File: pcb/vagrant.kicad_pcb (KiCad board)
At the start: 2 copper layers, 169.5 x 90.2 mm, 35 parts, among them K1 KEYSW, K10 KEYSW, K2 KEYSW, K3 KEYSW, K4 KEYSW, K5 KEYSW, K6 KEYSW, K7 KEYSW, K8 KEYSW, K9 KEYSW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

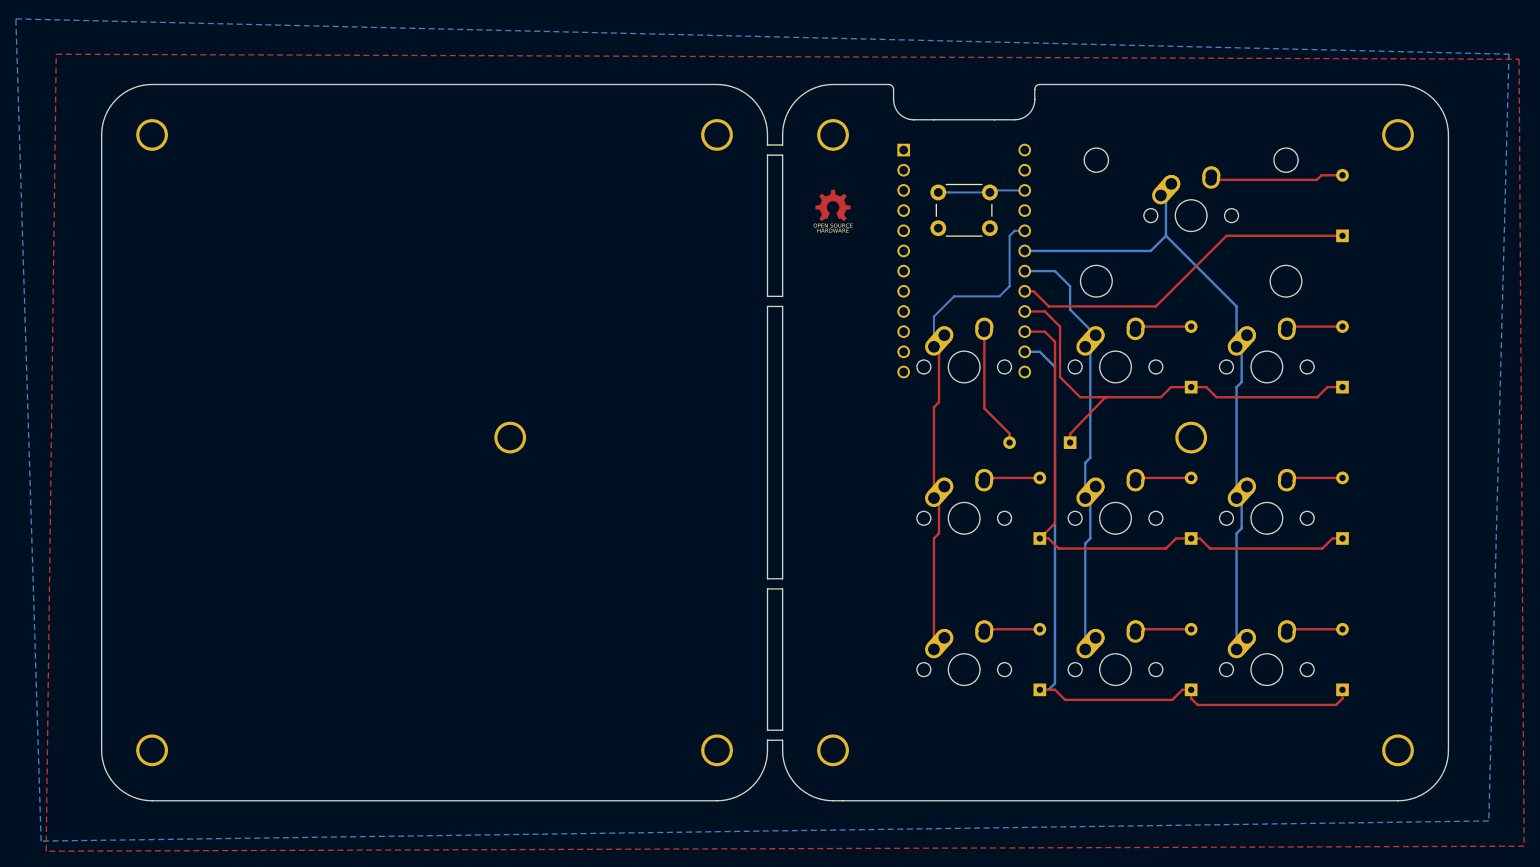
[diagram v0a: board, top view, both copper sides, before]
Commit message: minor changes on silk
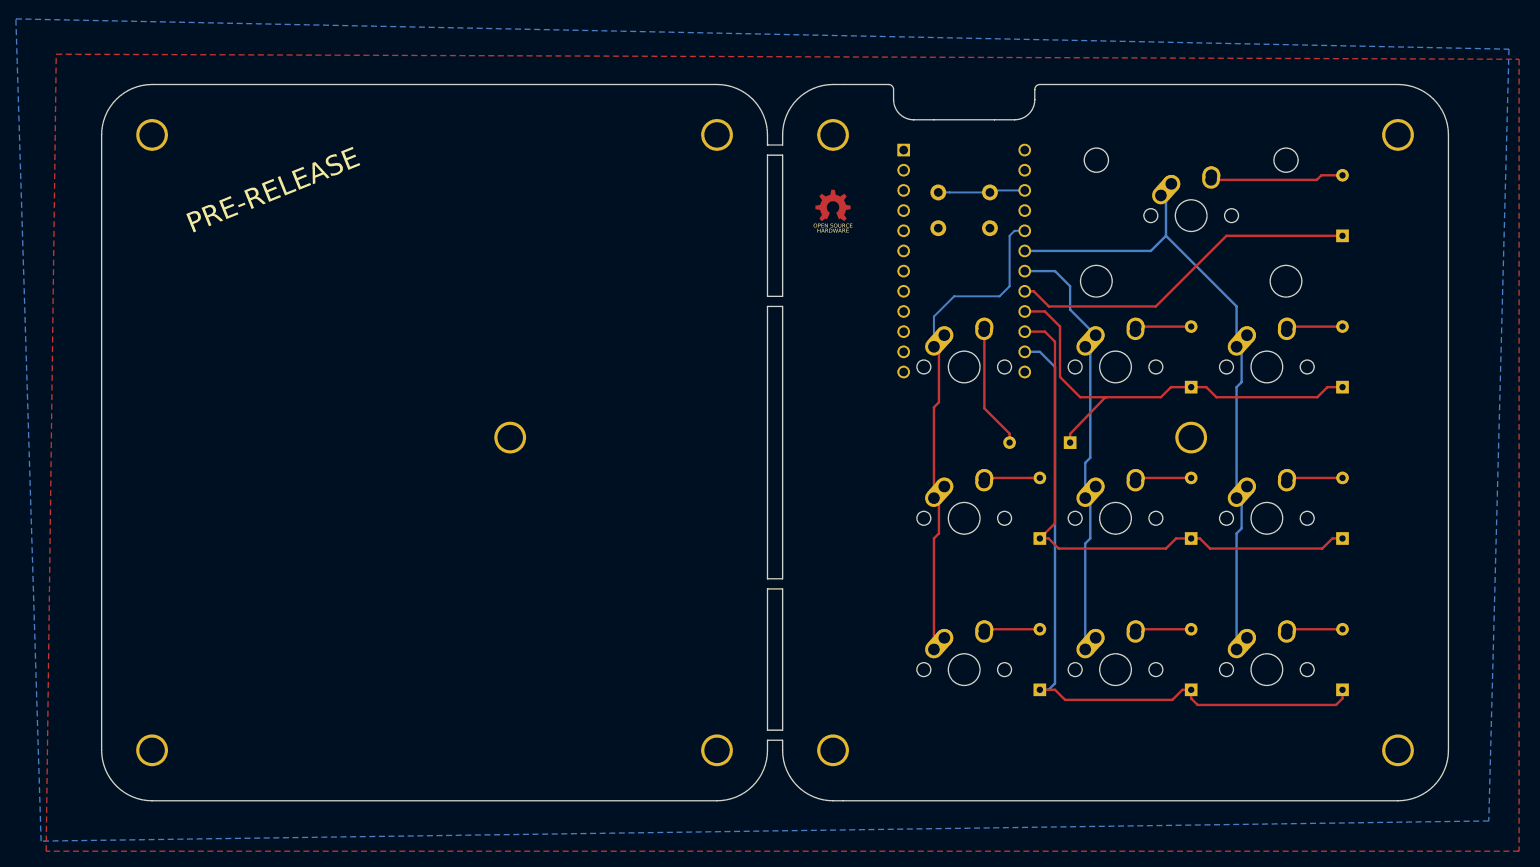
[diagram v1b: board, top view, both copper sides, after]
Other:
- board text added: "PRE-RELEASE"
- board text added: "Vagrant v0.2"
- board text removed: "Vagrant v0.1"

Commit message: Fixup space between parts
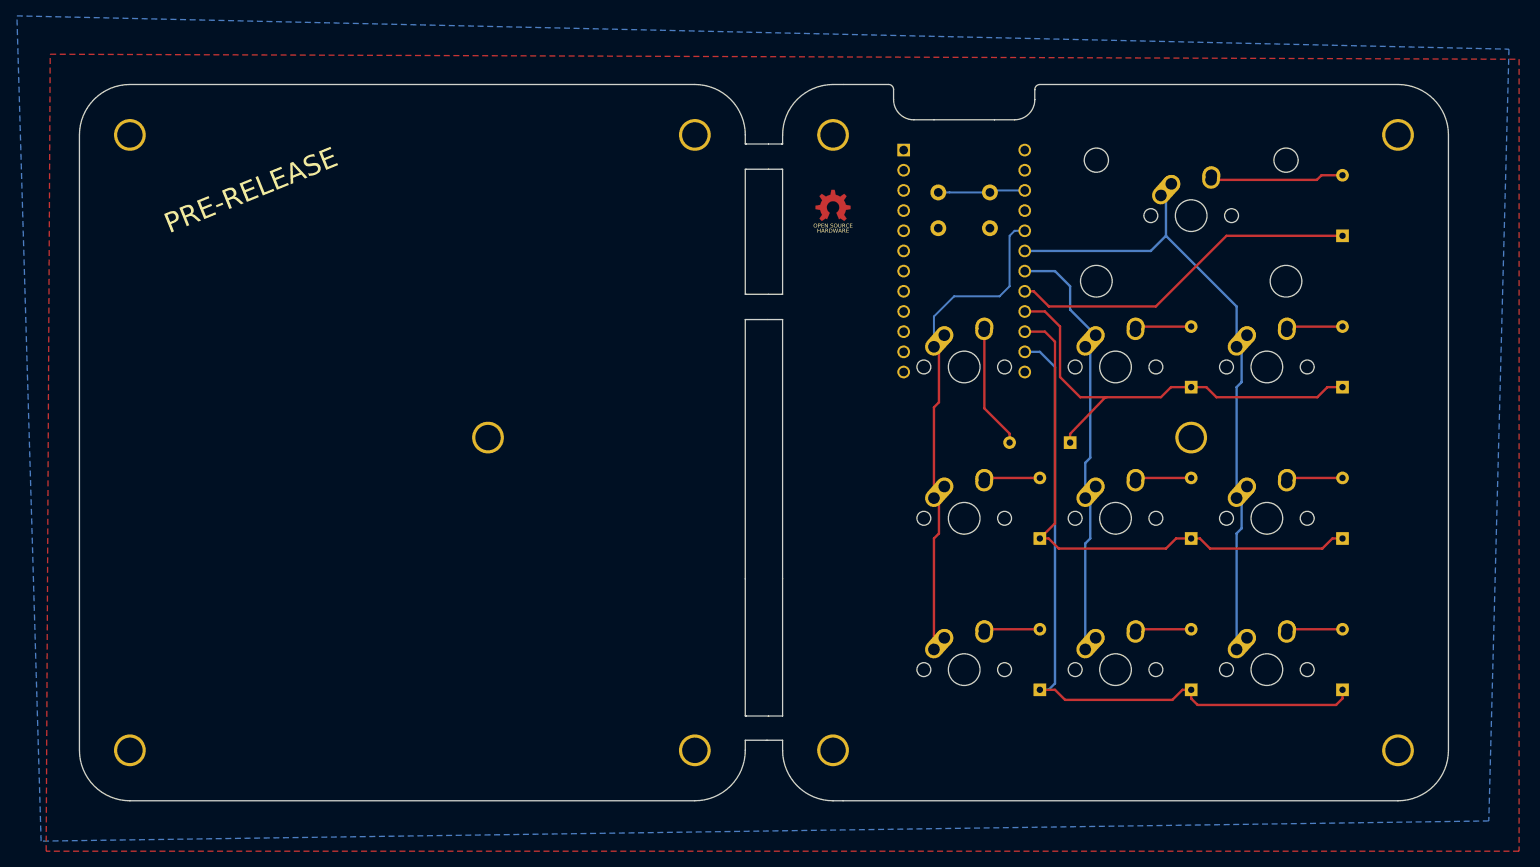
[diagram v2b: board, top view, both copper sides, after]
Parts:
- removed the HOLE_M3 at (110.5, 74.9)
- removed the HOLE_M3 at (65.4, 114.3)
- removed the HOLE_M3 at (136.5, 114.3)
- removed the HOLE_M3 at (136.5, 36.8)
- removed the HOLE_M3 at (65.4, 36.8)
- added HOLE_M3: VAL**, keyboard_parts:HOLE_M3, F.Cu at (107.7, 74.9)
- added HOLE_M3: VAL**, keyboard_parts:HOLE_M3, F.Cu at (62.6, 114.3)
- added HOLE_M3: VAL**, keyboard_parts:HOLE_M3, F.Cu at (133.7, 114.3)
- added HOLE_M3: VAL**, keyboard_parts:HOLE_M3, F.Cu at (133.7, 36.8)
- added HOLE_M3: VAL**, keyboard_parts:HOLE_M3, F.Cu at (62.6, 36.8)
- moved G*** 2.79 mm to (95.0, 75.6)
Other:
- board size 169.5 x 90.2 mm -> 172.3 x 90.2 mm
- board text added: "Vagrant v0.3"
- board text removed: "Vagrant v0.2"
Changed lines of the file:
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@@
   (general
     (thickness 1.6)
-    (drawings 50)
+    (drawings 62)
     (tracks 118)
     (zones 0)
@@
   )
   (page A4)
+  (title_block
+    (date 2020-03-08)
+  )
   (layers
-    (0 F.Cu signal)
-    (31 B.Cu signal)
+    (0 F.Cu signal hide)
+    (31 B.Cu signal hide)
     (32 B.Adhes user)
     (33 F.Adhes user)
@@
   )
   (module keyboard_parts:HOLE_M3 (layer F.Cu)
-    (at 65.405 114.3)
+    (at 62.611 114.3)
     (fp_text reference HOLE_M3 (at 0 -4.5) (layer F.SilkS) hide
       (effects (font (size 1.524 1.524) (thickness 0.3048)))
@@
   )
   (module keyboard_parts:HOLE_M3 (layer F.Cu)
-    (at 136.525 114.3)
+    (at 133.731 114.3)
     (fp_text reference HOLE_M3 (at 0 -4.5) (layer F.SilkS) hide
       (effects (font (size 1.524 1.524) (thickness 0.3048)))
@@
   )
   (module keyboard_parts:HOLE_M3 (layer F.Cu)
-    (at 136.525 36.83)
+    (at 133.731 36.83)
     (fp_text reference HOLE_M3 (at 0 -4.5) (layer F.SilkS) hide
       (effects (font (size 1.524 1.524) (thickness 0.3048)))
@@
   )
   (module keyboard_parts:HOLE_M3 (layer F.Cu)
-    (at 65.405 36.83)
+    (at 62.611 36.83)
     (fp_text reference HOLE_M3 (at 0 -4.5) (layer F.SilkS) hide
       (effects (font (size 1.524 1.524) (thickness 0.3048)))
@@
   )
   (module keyboard_parts:HOLE_M3 (layer F.Cu)
-    (at 110.49 74.93)
+    (at 107.696 74.93)
     (fp_text reference HOLE_M3 (at 0 -4.5) (layer F.SilkS) hide
       (effects (font (size 1.524 1.524) (thickness 0.3048)))
@@
   )
   (module logos:laughing_man (layer B.Cu)
-    (at 97.79 75.565 180)
+    (at 94.996 75.565 180)
     (fp_text reference G*** (at 0 0) (layer B.SilkS) hide
       (effects (font (size 1.524 1.524) (thickness 0.3)) (justify mirror))
@@
     )
   )
-  (gr_text PRE-RELEASE (at 80.645 43.815 22) (layer F.SilkS)
+  (gr_line (start 143.002 41.148) (end 140.208 41.148) (layer Edge.Cuts) (width 0.05))
+  (gr_line (start 143.002 37.973) (end 140.208 37.973) (layer Edge.Cuts) (width 0.05))
+  (gr_line (start 143.002 56.896) (end 140.208 56.896) (layer Edge.Cuts) (width 0.05))
+  (gr_line (start 142.875 60.071) (end 140.081 60.071) (layer Edge.Cuts) (width 0.05))
+  (gr_line (start 143.002 109.982) (end 140.208 109.982) (layer Edge.Cuts) (width 0.05))
+  (gr_line (start 142.748 113.03) (end 142.875 113.03) (layer Edge.Cuts) (width 0.05))
+  (gr_line (start 142.748 113.03) (end 140.081 113.03) (layer Edge.Cuts) (width 0.05))
+  (gr_line (start 140.081 60.071) (end 140.081 92.71) (layer Edge.Cuts) (width 0.05))
+  (gr_line (start 144.78 92.71) (end 144.78 60.071) (layer Edge.Cuts) (width 0.05))
+  (gr_line (start 140.081 56.896) (end 140.081 41.148) (layer Edge.Cuts) (width 0.05))
+  (gr_line (start 140.208 56.896) (end 140.081 56.896) (layer Edge.Cuts) (width 0.05))
+  (gr_line (start 144.78 56.896) (end 144.653 56.896) (layer Edge.Cuts) (width 0.05))
+  (gr_line (start 144.78 41.148) (end 144.78 56.896) (layer Edge.Cuts) (width 0.05))
+  (gr_line (start 144.653 41.148) (end 144.78 41.148) (layer Edge.Cuts) (width 0.05))
+  (gr_line (start 140.081 41.148) (end 140.208 41.148) (layer Edge.Cuts) (width 0.05))
+  (gr_line (start 140.081 37.973) (end 140.081 36.83) (layer Edge.Cuts) (width 0.05))
+  (gr_line (start 140.208 37.973) (end 140.081 37.973) (layer Edge.Cuts) (width 0.05))
+  (gr_line (start 144.78 37.973) (end 144.653 37.973) (layer Edge.Cuts) (width 0.05))
+  (gr_line (start 144.78 36.83) (end 144.78 37.973) (layer Edge.Cuts) (width 0.05))
+  (gr_line (start 144.653 37.973) (end 143.002 37.973) (layer Edge.Cuts) (width 0.05))
+  (gr_line (start 144.653 41.148) (end 143.002 41.148) (layer Edge.Cuts) (width 0.05))
+  (gr_line (start 143.002 56.896) (end 144.653 56.896) (layer Edge.Cuts) (width 0.05))
+  (gr_line (start 144.78 60.071) (end 142.875 60.071) (layer Edge.Cuts) (width 0.05))
+  (gr_line (start 144.78 92.71) (end 144.78 109.982) (layer Edge.Cuts) (width 0.05))
+  (gr_line (start 140.081 109.982) (end 140.081 92.71) (layer Edge.Cuts) (width 0.05))
+  (gr_line (start 140.208 109.982) (end 140.081 109.982) (layer Edge.Cuts) (width 0.05))
+  (gr_line (start 144.78 109.982) (end 143.002 109.982) (layer Edge.Cuts) (width 0.05))
+  (gr_line (start 144.78 113.03) (end 142.875 113.03) (layer Edge.Cuts) (width 0.05))
+  (gr_text PRE-RELEASE (at 77.851 43.815 22) (layer F.SilkS)
     (effects (font (size 2.5 2.5) (thickness 0.625)))
   )
@@
     (effects (font (size 2.5 2.5) (thickness 0.625)) (justify mirror))
   )
-  (gr_line (start 142.875 92.71) (end 142.875 58.42) (layer Edge.Cuts) (width 0.05))
-  (gr_line (start 144.78 92.71) (end 142.875 92.71) (layer Edge.Cuts) (width 0.05))
-  (gr_line (start 144.78 58.42) (end 144.78 92.71) (layer Edge.Cuts) (width 0.05))
-  (gr_line (start 144.78 39.37) (end 144.78 57.15) (layer Edge.Cuts) (width 0.05))
-  (gr_line (start 142.875 57.15) (end 142.875 39.37) (layer Edge.Cuts) (width 0.05))
-  (gr_line (start 144.78 93.98) (end 144.78 111.76) (layer Edge.Cuts) (width 0.05))
-  (gr_line (start 142.875 111.76) (end 142.875 93.98) (layer Edge.Cuts) (width 0.05))
-  (gr_line (start 144.78 111.76) (end 142.875 111.76) (layer Edge.Cuts) (width 0.05))
-  (gr_line (start 142.875 93.98) (end 144.78 93.98) (layer Edge.Cuts) (width 0.05))
-  (gr_line (start 142.875 58.42) (end 144.78 58.42) (layer Edge.Cuts) (width 0.05))
-  (gr_line (start 142.875 57.15) (end 144.78 57.15) (layer Edge.Cuts) (width 0.05))
-  (gr_line (start 142.875 39.37) (end 144.78 39.37) (layer Edge.Cuts) (width 0.05))
-  (gr_line (start 65.405 30.48) (end 136.525 30.48) (layer Edge.Cuts) (width 0.05))
-  (gr_line (start 59.055 114.3) (end 59.055 36.83) (layer Edge.Cuts) (width 0.05))
-  (gr_line (start 136.525 120.65) (end 65.405 120.65) (layer Edge.Cuts) (width 0.05))
-  (gr_line (start 142.875 113.03) (end 142.875 114.3) (layer Edge.Cuts) (width 0.05))
-  (gr_line (start 144.78 113.03) (end 142.875 113.03) (layer Edge.Cuts) (width 0.05))
+  (gr_line (start 62.611 30.48) (end 133.731 30.48) (layer Edge.Cuts) (width 0.05))
+  (gr_line (start 56.261 114.3) (end 56.261 36.83) (layer Edge.Cuts) (width 0.05))
+  (gr_line (start 133.731 120.65) (end 62.611 120.65) (layer Edge.Cuts) (width 0.05))
+  (gr_line (start 140.081 113.03) (end 140.081 114.3) (layer Edge.Cuts) (width 0.05))
   (gr_line (start 144.78 114.3) (end 144.78 113.03) (layer Edge.Cuts) (width 0.05))
-  (gr_line (start 142.875 38.1) (end 142.875 36.83) (layer Edge.Cuts) (width 0.05))
-  (gr_line (start 144.78 38.1) (end 142.875 38.1) (layer Edge.Cuts) (width 0.05))
-  (gr_arc (start 65.405 114.3) (end 59.055 114.3) (angle -90) (layer Edge.Cuts) (width 0.05))
-  (gr_arc (start 65.405 36.83) (end 65.405 30.48) (angle -90) (layer Edge.Cuts) (width 0.05))
-  (gr_arc (start 136.525 114.3) (end 136.525 120.65) (angle -90) (layer Edge.Cuts) (width 0.05))
-  (gr_arc (start 136.525 36.83) (end 142.875 36.83) (angle -90) (layer Edge.Cuts) (width 0.05))
+  (gr_arc (start 62.611 114.3) (end 56.261 114.3) (angle -90) (layer Edge.Cuts) (width 0.05))
+  (gr_arc (start 62.611 36.83) (end 62.611 30.48) (angle -90) (layer Edge.Cuts) (width 0.05))
+  (gr_arc (start 133.731 114.3) (end 133.731 120.65) (angle -90) (layer Edge.Cuts) (width 0.05))
+  (gr_arc (start 133.731 36.83) (end 140.081 36.83) (angle -90) (layer Edge.Cuts) (width 0.05))
   (gr_text "HARDWARE\n" (at 151.13 48.895) (layer F.SilkS)
     (effects (font (size 0.5 0.5) (thickness 0.125)))
@@
     (effects (font (size 0.5 0.5) (thickness 0.125)))
   )
-  (gr_text "Vagrant v0.2\n" (at 196.215 33.655) (layer B.SilkS)
+  (gr_text "Vagrant v0.3\n" (at 196.215 33.655) (layer B.SilkS)
     (effects (font (size 1.5 1.5) (thickness 0.375)) (justify mirror))
   )
@@
   (gr_arc (start 161.29 32.385) (end 158.75 32.385) (angle -90) (layer Edge.Cuts) (width 0.05))
   (gr_arc (start 158.115 31.115) (end 158.75 31.115) (angle -90) (layer Edge.Cuts) (width 0.05))
-  (gr_line (start 144.78 36.83) (end 144.78 38.1) (layer Edge.Cuts) (width 0.05))
   (gr_line (start 152.4 30.48) (end 151.13 30.48) (layer Edge.Cuts) (width 0.05))
   (gr_line (start 228.6 38.1) (end 228.6 36.83) (layer Edge.Cuts) (width 0.05))
@@
     (polygon
       (pts
-        (xy 237.49 127) (xy 52.07 127) (xy 53.34 26.67) (xy 237.49 27.305)
+        (xy 237.49 127) (xy 52.07 127) (xy 52.578 26.67) (xy 237.49 27.305)
       )
     )
@@
     (polygon
       (pts
-        (xy 233.68 123.19) (xy 51.435 125.73) (xy 48.26 22.225) (xy 236.22 26.035)
+        (xy 233.68 123.19) (xy 51.435 125.73) (xy 48.387 21.844) (xy 236.22 26.035)
       )
     )
